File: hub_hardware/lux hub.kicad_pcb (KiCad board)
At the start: 4 copper layers, 105.4 x 57.1 mm, 136 parts, among them CON1 48V, CON2 USB-MINI-B, P1 CONN_4, P2 CONN_4, P3 CONN_4, P4 CONN_4, P5 CONN_4, P6 CONN_4, P7 CONN_4, Q1 DMP6023LE-13, Q10 BC856BLT, Q11 BTX54CTU, Q12 BC856BLT, Q13 BTX54CTU, Q2 BC856BLT, Q3 BTX54CTU, Q4 BC856BLT, Q5 BTX54CTU, Q6 BC856BLT, Q7 BTX54CTU, Q8 BC856BLT, Q9 BTX54CTU, SW1 BOOT, U1 3V3REG, U10 ISL83485IBZ, U11 2CH-TVS, U12 ISL83485IBZ, U13 2CH-TVS, U14 ISL83485IBZ, U15 2CH-TVS, U2 STM32F042-32, U3 4068, U4 ISL83485IBZ, U5 2CH-TVS, U6 ISL83485IBZ, U7 2CH-TVS, U8 ISL83485IBZ, U9 2CH-TVS

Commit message: Lux Hub v8
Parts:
- removed C1, C13: 100n, Capacitors_SMD:C_0402
- removed D11, D13, D3, D5, D7, D9: ENABLED, custom:LED_0603_flipped
- removed Q1: DMP6023LE-13, SOT223
- removed Q10, Q12, Q2, Q4, Q6, Q8: BC856BLT, TO_SOT_Packages_SMD:SOT-23
- removed Q11, Q13, Q3, Q5, Q7, Q9: BTX54CTU, TO_SOT_Packages_THT:TO-220-3_Vertical
- removed R1: 100K, Resistors_SMD:R_0402
- removed R10, R22, R28, R40, R51, R53, R54, R56, R57, R59, R60, R62: 10K, Resistors_SMD:R_0402
- removed R12, R18, R24, R30, R36, R6: 470R, Resistors_SMD:R_0402
- removed R16, R34, R52, R55, R58, R61: 2, Resistors_SMD:R_2512
- removed R42: 120R, Resistors_SMD:R_0402
- removed REF: SolderWirePad_single_2mmDrill, Wire_Pads:SolderWirePad_single_2mmDrill
- removed the REF** at (27.4, 70.1)
- removed the REF** at (126.5, 70.1)
- removed the REF** at (126.5, 120.9)
- added REF**: MountingHole_2.7mm_M2.5_ISO14580_Pad, Mounting_Holes:MountingHole_2.7mm_M2.5_ISO14580_Pad, F.Cu at (27.9, 76.7)
- added REF**: MountingHole_2.7mm_M2.5_ISO14580_Pad, Mounting_Holes:MountingHole_2.7mm_M2.5_ISO14580_Pad, F.Cu at (28.2, 119.9)
- added REF**: MountingHole_2.7mm_M2.5_ISO14580_Pad, Mounting_Holes:MountingHole_2.7mm_M2.5_ISO14580_Pad, F.Cu at (125.2, 119.6)
- added REF**: MountingHole_2.7mm_M2.5_ISO14580_Pad, Mounting_Holes:MountingHole_2.7mm_M2.5_ISO14580_Pad, F.Cu at (125.5, 76.5)
- added U16: BTS4175SGA, SMD_Packages:SOIC-8-N, F.Cu at (43.7, 89.4)
- added U17: BTS4175SGA, SMD_Packages:SOIC-8-N, F.Cu at (57.9, 89.4)
- added U18: BTS4175SGA, SMD_Packages:SOIC-8-N, F.Cu at (72.1, 89.4)
- added U19: BTS4175SGA, SMD_Packages:SOIC-8-N, F.Cu at (86.4, 89.4)
- added U20: BTS4175SGA, SMD_Packages:SOIC-8-N, F.Cu at (100.6, 89.4)
- added U21: BTS4175SGA, SMD_Packages:SOIC-8-N, F.Cu at (114.8, 89.4)
- C10, C11, C12, C14, C5, C6, C7, C8, C9: footprint Capacitors_SMD:C_0402 -> Capacitors_SMD:C_0603
- D1, D10, D12, D14, D15, D16, D2, D4, D6, D8: footprint custom:LED_0603_flipped -> LEDs:LED_0603
- R4, R43, R44, R45, R46, R47, R48, R49, R5: footprint Resistors_SMD:R_0402 -> Resistors_SMD:R_0603
- moved R3 27.8 mm to (125.2, 90.4)
- moved U11 6.35 mm to (79.2, 89.9)
- moved U13 6.35 mm to (93.5, 89.9)
- moved U15 6.35 mm to (107.7, 89.9)
- moved U5 6.35 mm to (36.6, 89.9)
- moved U7 6.35 mm to (50.8, 89.9)
- moved U9 6.35 mm to (65.0, 89.9)
- moved P1 5.08 mm to (41.7, 74.7)
- moved P2 5.08 mm to (55.9, 74.7)
- moved P3 5.08 mm to (70.1, 74.7)
- moved P4 5.08 mm to (84.3, 74.7)
- moved P5 5.08 mm to (98.6, 74.7)
- moved P6 5.08 mm to (112.8, 74.7)
- moved R29 4.38 mm to (84.1, 94.2), turned to 0 degrees
- moved R35 4.38 mm to (98.3, 94.2), turned to 0 degrees
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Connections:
- F1 pad 2: Net-(C1-Pad1) -> +48V
- R3 pad 1: GND -> /DE3
- R3 pad 2: /DE3 -> GND
- U2 pad 10: /LED2 -> /PWR2
- U2 pad 11: /LED3 -> /PWR3
- U2 pad 12: /LED4 -> /PWR4
- U2 pad 13: /LED5 -> /PWR5
- U2 pad 14: /LED6 -> /PWR6
- U2 pad 9: /LED1 -> /PWR1
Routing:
- net /PWR6: track 0.00 -> 131.0 mm, vias 0 -> 2
- net /LED6: track 129.0 -> 0.00 mm, vias 2 -> 0
- net /PWR5: track 0.00 -> 115.5 mm, vias 0 -> 2
- net /LED5: track 113.4 -> 0.00 mm, vias 2 -> 0
- net /PWR4: track 0.00 -> 101.2 mm, vias 0 -> 2
- net /LED4: track 99.2 -> 0.00 mm, vias 2 -> 0
- net /PWR1: track 0.00 -> 92.7 mm, vias 0 -> 2
- net /PWR3: track 0.00 -> 87.7 mm, vias 0 -> 2
- net /LED1: track 86.9 -> 0.00 mm, vias 2 -> 0
- net /LED3: track 85.3 -> 0.00 mm, vias 2 -> 0
- net /PWR2: track 0.00 -> 81.4 mm, vias 0 -> 2
- net /LED2: track 78.1 -> 0.00 mm, vias 2 -> 0
- net Net-(C1-Pad1): track 27.6 -> 0.00 mm
- net GND: track 115.4 -> 90.6 mm, vias 40 -> 31
- net Net-(C1-Pad2): track 22.3 -> 0.00 mm, vias 3 -> 0
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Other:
- board size 105.4 x 57.1 mm -> 105.4 x 52.1 mm
- board text added: "12V-48V"
- board text added: "Lux Hub rev 8"
- board text added: "Lux Hub rev 8 https://github.com/ervanalb/lux"
- board text removed: "12V-48V, 5A"
- board text removed: "EN"
- board text removed: "Lux Hub rev 7"
- board text removed: "Lux Hub rev 7 https://github.com/ervanalb/lux"

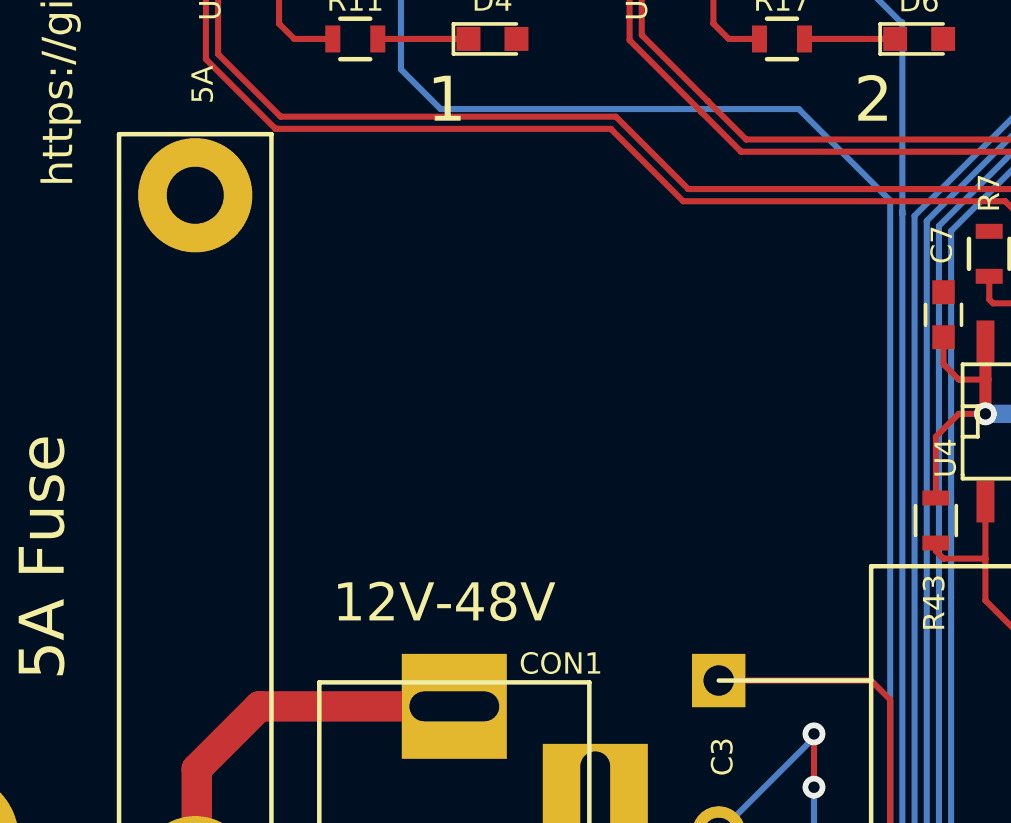
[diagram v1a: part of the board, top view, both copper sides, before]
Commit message: Add soft-start circuit to lux hub v8, update gerbers
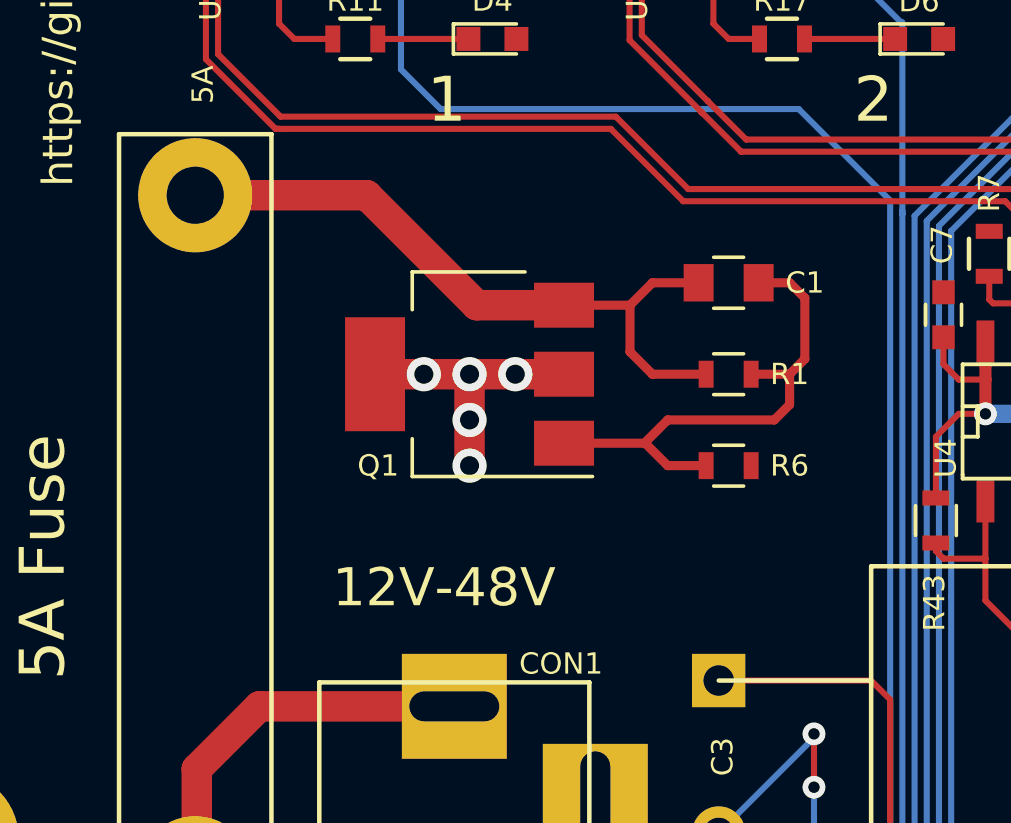
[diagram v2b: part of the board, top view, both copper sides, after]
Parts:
- added C1: 1u, Capacitors_SMD:C_0805, F.Cu at (53.8, 102.1)
- added Q1: DMP6023LE, TO_SOT_Packages_SMD:SOT-223-3_TabPin2, F.Cu at (45.2, 105.2)
- added R1: 100K, Resistors_SMD:R_0603, F.Cu at (53.8, 105.2)
- added R6: 390K, Resistors_SMD:R_0603, F.Cu at (53.8, 108.2)
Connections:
- F1 pad 2: +48V -> Net-(C1-Pad1)
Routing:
- net Net-(C1-Pad1): track 0.00 -> 23.0 mm
- net Net-(C1-Pad2): track 0.00 -> 17.2 mm
- net +48V: track 84.1 -> 93.5 mm, vias 25 -> 30
- net GND: vias 31 -> 30
- net (no net): vias 0 -> 1
